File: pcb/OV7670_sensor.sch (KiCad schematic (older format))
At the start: 2 parts, among them U5 OV7670_module, U6 OV7670_module

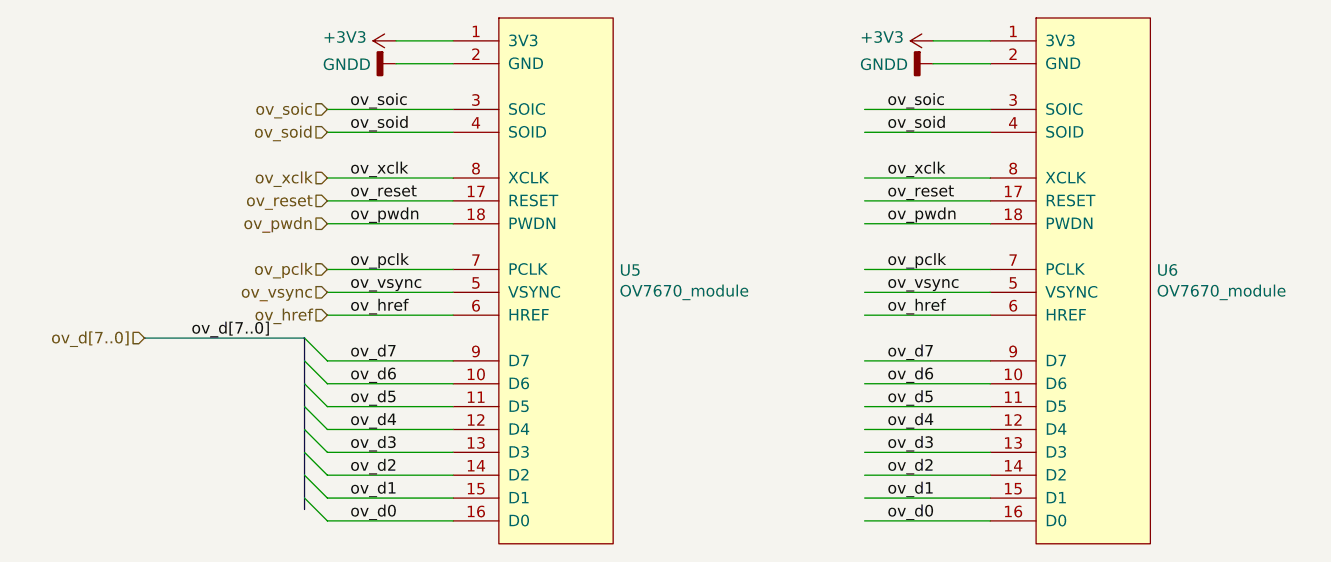
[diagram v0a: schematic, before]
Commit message: OV flat footprint
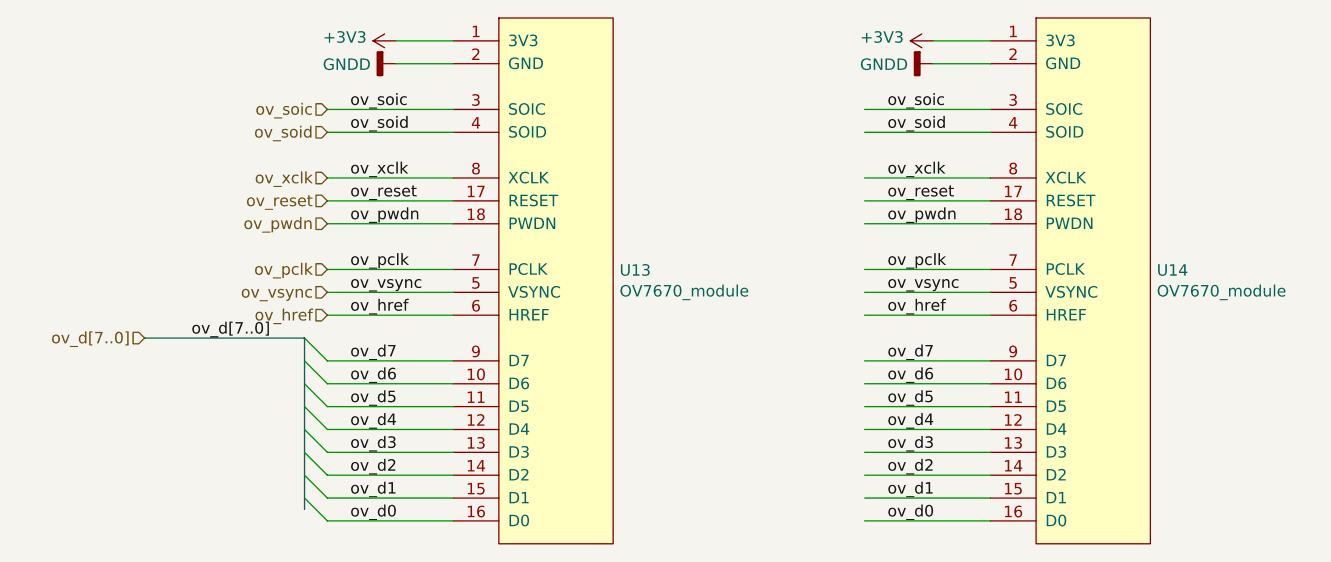
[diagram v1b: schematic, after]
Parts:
- U5: footprint Connector_PinSocket_2.54mm:PinSocket_2x09_P2.54mm_Horizontal -> OV7670_Module:OV7670_Flat
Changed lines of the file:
@@
 AR Path="/5C9B2A05/5C9B36DA" Ref="U5"  Part="1"
 AR Path="/5C9C0506/5C9B36DA" Ref="U7"  Part="1"
-AR Path="/5C9C8588/5C9B36DA" Ref="U?"  Part="1"
-AR Path="/5C9C95E9/5C9B36DA" Ref="U?"  Part="1"
-AR Path="/5C9CA91D/5C9B36DA" Ref="U?"  Part="1"
-AR Path="/5C9CA93A/5C9B36DA" Ref="U?"  Part="1"
-AR Path="/5C9CA957/5C9B36DA" Ref="U?"  Part="1"
-AR Path="/5C9CA974/5C9B36DA" Ref="U?"  Part="1"
-F 0 "U?" H 4578 3146 50  0000 L CNN
+AR Path="/5C9C8588/5C9B36DA" Ref="U9"  Part="1"
+AR Path="/5C9C95E9/5C9B36DA" Ref="U11"  Part="1"
+AR Path="/5C9CA91D/5C9B36DA" Ref="U13"  Part="1"
+AR Path="/5C9CA93A/5C9B36DA" Ref="U15"  Part="1"
+AR Path="/5C9CA957/5C9B36DA" Ref="U17"  Part="1"
+AR Path="/5C9CA974/5C9B36DA" Ref="U19"  Part="1"
+F 0 "U13" H 4578 3146 50  0000 L CNN
 F 1 "OV7670_module" H 4578 3055 50  0000 L CNN
-F 2 "Connector_PinSocket_2.54mm:PinSocket_2x09_P2.54mm_Horizontal" H 4150 4200 50  0001 C CNN
+F 2 "OV7670_Module:OV7670_Flat" H 4150 4200 50  0001 C CNN
 F 3 "" H 4150 4200 50  0001 C CNN
 	1    4150 2950
@@
 AR Path="/5C9B2A05/5C9B3748" Ref="#PWR0110"  Part="1"
 AR Path="/5C9C0506/5C9B3748" Ref="#PWR018"  Part="1"
-AR Path="/5C9C8588/5C9B3748" Ref="#PWR?"  Part="1"
-AR Path="/5C9C95E9/5C9B3748" Ref="#PWR?"  Part="1"
-AR Path="/5C9CA91D/5C9B3748" Ref="#PWR?"  Part="1"
-AR Path="/5C9CA93A/5C9B3748" Ref="#PWR?"  Part="1"
-AR Path="/5C9CA957/5C9B3748" Ref="#PWR?"  Part="1"
-AR Path="/5C9CA974/5C9B3748" Ref="#PWR?"  Part="1"
-F 0 "#PWR?" H 3600 1600 50  0001 C CNN
+AR Path="/5C9C8588/5C9B3748" Ref="#PWR0114"  Part="1"
+AR Path="/5C9C95E9/5C9B3748" Ref="#PWR0118"  Part="1"
+AR Path="/5C9CA91D/5C9B3748" Ref="#PWR0122"  Part="1"
+AR Path="/5C9CA93A/5C9B3748" Ref="#PWR0126"  Part="1"
+AR Path="/5C9CA957/5C9B3748" Ref="#PWR0130"  Part="1"
+AR Path="/5C9CA974/5C9B3748" Ref="#PWR0134"  Part="1"
+F 0 "#PWR0122" H 3600 1600 50  0001 C CNN
 F 1 "GNDD" V 3604 1740 50  0000 R CNN
 F 2 "" H 3600 1850 50  0001 C CNN
@@
 AR Path="/5C9B2A05/5C9B37B4" Ref="#PWR0111"  Part="1"
 AR Path="/5C9C0506/5C9B37B4" Ref="#PWR014"  Part="1"
-AR Path="/5C9C8588/5C9B37B4" Ref="#PWR?"  Part="1"
-AR Path="/5C9C95E9/5C9B37B4" Ref="#PWR?"  Part="1"
-AR Path="/5C9CA91D/5C9B37B4" Ref="#PWR?"  Part="1"
-AR Path="/5C9CA93A/5C9B37B4" Ref="#PWR?"  Part="1"
-AR Path="/5C9CA957/5C9B37B4" Ref="#PWR?"  Part="1"
-AR Path="/5C9CA974/5C9B37B4" Ref="#PWR?"  Part="1"
-F 0 "#PWR?" H 3600 1600 50  0001 C CNN
+AR Path="/5C9C8588/5C9B37B4" Ref="#PWR0115"  Part="1"
+AR Path="/5C9C95E9/5C9B37B4" Ref="#PWR0119"  Part="1"
+AR Path="/5C9CA91D/5C9B37B4" Ref="#PWR0123"  Part="1"
+AR Path="/5C9CA93A/5C9B37B4" Ref="#PWR0127"  Part="1"
+AR Path="/5C9CA957/5C9B37B4" Ref="#PWR0131"  Part="1"
+AR Path="/5C9CA974/5C9B37B4" Ref="#PWR0135"  Part="1"
+F 0 "#PWR0123" H 3600 1600 50  0001 C CNN
 F 1 "+3V3" V 3615 1878 50  0000 L CNN
 F 2 "" H 3600 1750 50  0001 C CNN
@@
 AR Path="/5C9B2A05/5C9B9810" Ref="U6"  Part="1"
 AR Path="/5C9C0506/5C9B9810" Ref="U8"  Part="1"
-AR Path="/5C9C8588/5C9B9810" Ref="U?"  Part="1"
-AR Path="/5C9C95E9/5C9B9810" Ref="U?"  Part="1"
-AR Path="/5C9CA91D/5C9B9810" Ref="U?"  Part="1"
-AR Path="/5C9CA93A/5C9B9810" Ref="U?"  Part="1"
-AR Path="/5C9CA957/5C9B9810" Ref="U?"  Part="1"
-AR Path="/5C9CA974/5C9B9810" Ref="U?"  Part="1"
-F 0 "U?" H 6928 3146 50  0000 L CNN
+AR Path="/5C9C8588/5C9B9810" Ref="U10"  Part="1"
+AR Path="/5C9C95E9/5C9B9810" Ref="U12"  Part="1"
+AR Path="/5C9CA91D/5C9B9810" Ref="U14"  Part="1"
+AR Path="/5C9CA93A/5C9B9810" Ref="U16"  Part="1"
+AR Path="/5C9CA957/5C9B9810" Ref="U18"  Part="1"
+AR Path="/5C9CA974/5C9B9810" Ref="U20"  Part="1"
+F 0 "U14" H 6928 3146 50  0000 L CNN
 F 1 "OV7670_module" H 6928 3055 50  0000 L CNN
 F 2 "Connector_PinSocket_2.54mm:PinSocket_2x09_P2.54mm_Vertical" H 6500 4200 50  0001 C CNN
@@
 AR Path="/5C9B2A05/5C9B9819" Ref="#PWR0112"  Part="1"
 AR Path="/5C9C0506/5C9B9819" Ref="#PWR020"  Part="1"
-AR Path="/5C9C8588/5C9B9819" Ref="#PWR?"  Part="1"
-AR Path="/5C9C95E9/5C9B9819" Ref="#PWR?"  Part="1"
-AR Path="/5C9CA91D/5C9B9819" Ref="#PWR?"  Part="1"
-AR Path="/5C9CA93A/5C9B9819" Ref="#PWR?"  Part="1"
-AR Path="/5C9CA957/5C9B9819" Ref="#PWR?"  Part="1"
-AR Path="/5C9CA974/5C9B9819" Ref="#PWR?"  Part="1"
-F 0 "#PWR?" H 5950 1600 50  0001 C CNN
+AR Path="/5C9C8588/5C9B9819" Ref="#PWR0116"  Part="1"
+AR Path="/5C9C95E9/5C9B9819" Ref="#PWR0120"  Part="1"
+AR Path="/5C9CA91D/5C9B9819" Ref="#PWR0124"  Part="1"
+AR Path="/5C9CA93A/5C9B9819" Ref="#PWR0128"  Part="1"
+AR Path="/5C9CA957/5C9B9819" Ref="#PWR0132"  Part="1"
+AR Path="/5C9CA974/5C9B9819" Ref="#PWR0136"  Part="1"
+F 0 "#PWR0124" H 5950 1600 50  0001 C CNN
 F 1 "GNDD" V 5954 1740 50  0000 R CNN
 F 2 "" H 5950 1850 50  0001 C CNN
@@
 AR Path="/5C9B2A05/5C9B981F" Ref="#PWR0113"  Part="1"
 AR Path="/5C9C0506/5C9B981F" Ref="#PWR019"  Part="1"
-AR Path="/5C9C8588/5C9B981F" Ref="#PWR?"  Part="1"
-AR Path="/5C9C95E9/5C9B981F" Ref="#PWR?"  Part="1"
-AR Path="/5C9CA91D/5C9B981F" Ref="#PWR?"  Part="1"
-AR Path="/5C9CA93A/5C9B981F" Ref="#PWR?"  Part="1"
-AR Path="/5C9CA957/5C9B981F" Ref="#PWR?"  Part="1"
-AR Path="/5C9CA974/5C9B981F" Ref="#PWR?"  Part="1"
-F 0 "#PWR?" H 5950 1600 50  0001 C CNN
+AR Path="/5C9C8588/5C9B981F" Ref="#PWR0117"  Part="1"
+AR Path="/5C9C95E9/5C9B981F" Ref="#PWR0121"  Part="1"
+AR Path="/5C9CA91D/5C9B981F" Ref="#PWR0125"  Part="1"
+AR Path="/5C9CA93A/5C9B981F" Ref="#PWR0129"  Part="1"
+AR Path="/5C9CA957/5C9B981F" Ref="#PWR0133"  Part="1"
+AR Path="/5C9CA974/5C9B981F" Ref="#PWR0137"  Part="1"
+F 0 "#PWR0125" H 5950 1600 50  0001 C CNN
 F 1 "+3V3" V 5965 1878 50  0000 L CNN
 F 2 "" H 5950 1750 50  0001 C CNN

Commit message: Cameras angled 22.5.
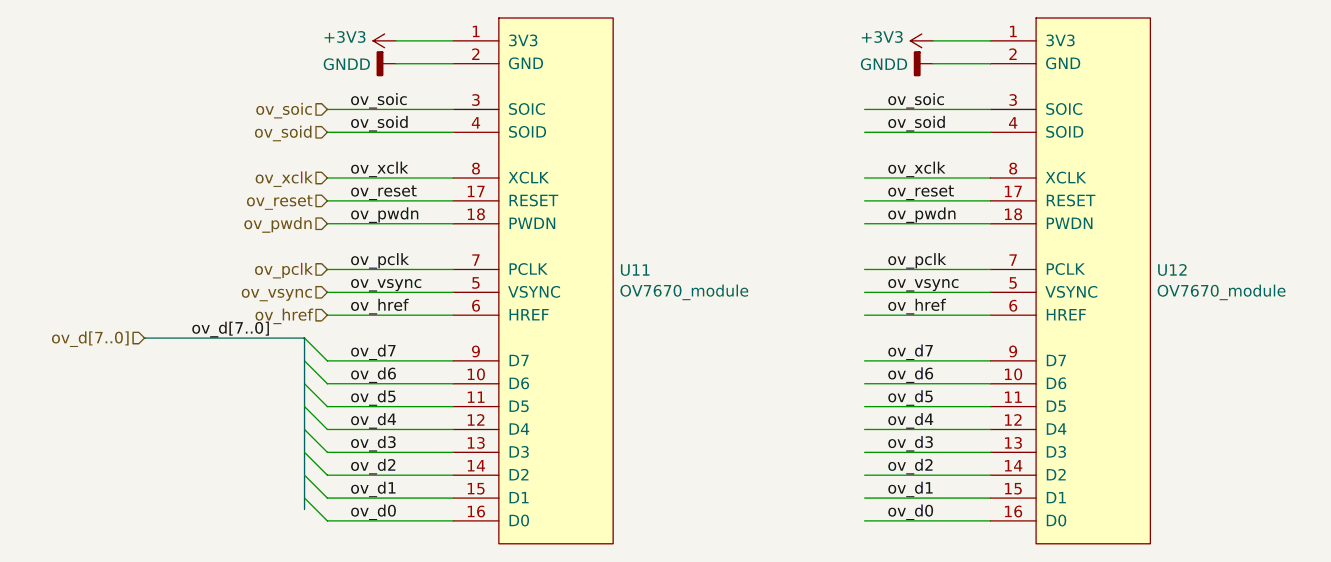
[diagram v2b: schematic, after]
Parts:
- U6: footprint Connector_PinSocket_2.54mm:PinSocket_2x09_P2.54mm_Vertical -> OV7670_Module:OV7670_Vertical
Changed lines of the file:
@@
 $Descr A4 11693 8268
 encoding utf-8
-Sheet 8 12
+Sheet 5 12
 Title ""
 Date ""
@@
 AR Path="/5C9CA957/5C9B36DA" Ref="U17"  Part="1"
 AR Path="/5C9CA974/5C9B36DA" Ref="U19"  Part="1"
-F 0 "U13" H 4578 3146 50  0000 L CNN
+F 0 "U11" H 4578 3146 50  0000 L CNN
 F 1 "OV7670_module" H 4578 3055 50  0000 L CNN
 F 2 "OV7670_Module:OV7670_Flat" H 4150 4200 50  0001 C CNN
@@
 AR Path="/5C9CA957/5C9B3748" Ref="#PWR0130"  Part="1"
 AR Path="/5C9CA974/5C9B3748" Ref="#PWR0134"  Part="1"
-F 0 "#PWR0122" H 3600 1600 50  0001 C CNN
+F 0 "#PWR0118" H 3600 1600 50  0001 C CNN
 F 1 "GNDD" V 3604 1740 50  0000 R CNN
 F 2 "" H 3600 1850 50  0001 C CNN
@@
 AR Path="/5C9CA957/5C9B37B4" Ref="#PWR0131"  Part="1"
 AR Path="/5C9CA974/5C9B37B4" Ref="#PWR0135"  Part="1"
-F 0 "#PWR0123" H 3600 1600 50  0001 C CNN
+F 0 "#PWR0119" H 3600 1600 50  0001 C CNN
 F 1 "+3V3" V 3615 1878 50  0000 L CNN
 F 2 "" H 3600 1750 50  0001 C CNN
@@
 AR Path="/5C9CA957/5C9B9810" Ref="U18"  Part="1"
 AR Path="/5C9CA974/5C9B9810" Ref="U20"  Part="1"
-F 0 "U14" H 6928 3146 50  0000 L CNN
+F 0 "U12" H 6928 3146 50  0000 L CNN
 F 1 "OV7670_module" H 6928 3055 50  0000 L CNN
-F 2 "Connector_PinSocket_2.54mm:PinSocket_2x09_P2.54mm_Vertical" H 6500 4200 50  0001 C CNN
+F 2 "OV7670_Module:OV7670_Vertical" H 6500 4200 50  0001 C CNN
 F 3 "" H 6500 4200 50  0001 C CNN
 	1    6500 2950
@@
 AR Path="/5C9CA957/5C9B9819" Ref="#PWR0132"  Part="1"
 AR Path="/5C9CA974/5C9B9819" Ref="#PWR0136"  Part="1"
-F 0 "#PWR0124" H 5950 1600 50  0001 C CNN
+F 0 "#PWR0120" H 5950 1600 50  0001 C CNN
 F 1 "GNDD" V 5954 1740 50  0000 R CNN
 F 2 "" H 5950 1850 50  0001 C CNN
@@
 AR Path="/5C9CA957/5C9B981F" Ref="#PWR0133"  Part="1"
 AR Path="/5C9CA974/5C9B981F" Ref="#PWR0137"  Part="1"
-F 0 "#PWR0125" H 5950 1600 50  0001 C CNN
+F 0 "#PWR0121" H 5950 1600 50  0001 C CNN
 F 1 "+3V3" V 5965 1878 50  0000 L CNN
 F 2 "" H 5950 1750 50  0001 C CNN

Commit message: Remove one flat sensor site.
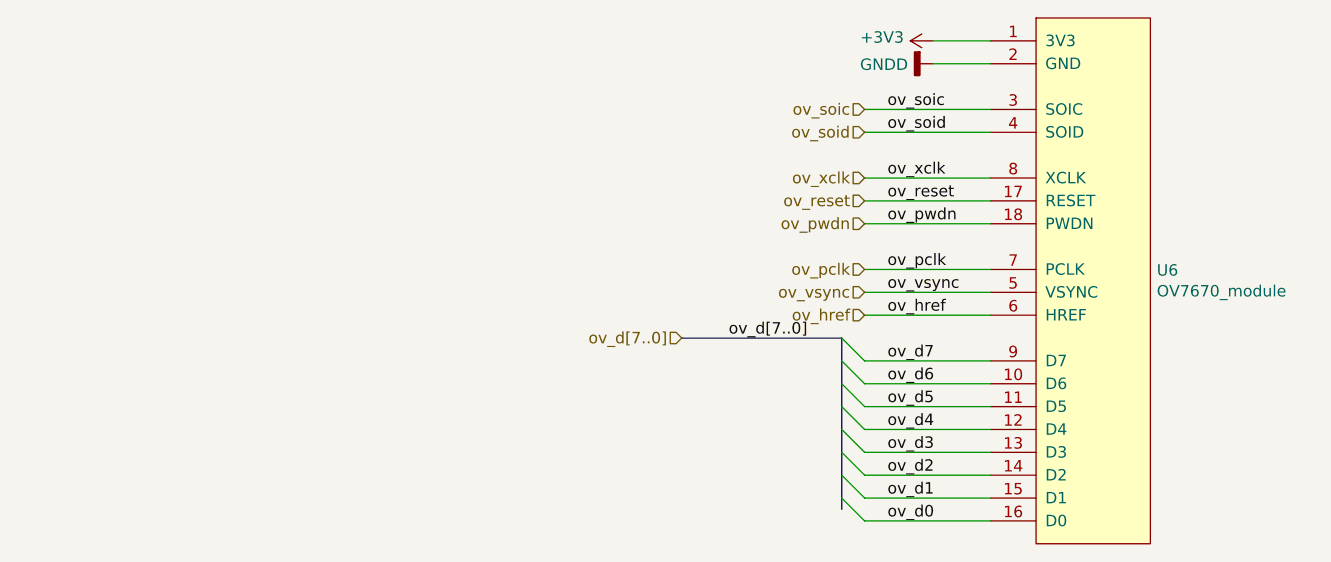
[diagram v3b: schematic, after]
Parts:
- removed U5: OV7670_module, OV7670_Module:OV7670_Flat, symbol OV7670:OV7670_module
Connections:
- wire segments 36 -> 18
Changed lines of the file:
@@
 $Descr A4 11693 8268
 encoding utf-8
-Sheet 5 12
+Sheet 5 11
 Title ""
 Date ""
@@
 Comment4 ""
 $EndDescr
-$Comp
-L OV7670:OV7670_module U5
-U 1 1 5C9B36DA
-P 4150 2950
-AR Path="/5C9B2A05/5C9B36DA" Ref="U5"  Part="1"
-AR Path="/5C9C0506/5C9B36DA" Ref="U7"  Part="1"
-AR Path="/5C9C8588/5C9B36DA" Ref="U9"  Part="1"
-AR Path="/5C9C95E9/5C9B36DA" Ref="U11"  Part="1"
-AR Path="/5C9CA91D/5C9B36DA" Ref="U13"  Part="1"
-AR Path="/5C9CA93A/5C9B36DA" Ref="U15"  Part="1"
-AR Path="/5C9CA957/5C9B36DA" Ref="U17"  Part="1"
-AR Path="/5C9CA974/5C9B36DA" Ref="U19"  Part="1"
-F 0 "U11" H 4578 3146 50  0000 L CNN
-F 1 "OV7670_module" H 4578 3055 50  0000 L CNN
-F 2 "OV7670_Module:OV7670_Flat" H 4150 4200 50  0001 C CNN
-F 3 "" H 4150 4200 50  0001 C CNN
-	1    4150 2950
-	1    0    0    -1
-$EndComp
-Wire Wire Line
-	3850 1750 3600 1750
-Wire Wire Line
-	3850 1850 3600 1850
-$Comp
-L power:GNDD #PWR0110
-U 1 1 5C9B3748
-P 3600 1850
-AR Path="/5C9B2A05/5C9B3748" Ref="#PWR0110"  Part="1"
-AR Path="/5C9C0506/5C9B3748" Ref="#PWR018"  Part="1"
-AR Path="/5C9C8588/5C9B3748" Ref="#PWR0114"  Part="1"
-AR Path="/5C9C95E9/5C9B3748" Ref="#PWR0118"  Part="1"
-AR Path="/5C9CA91D/5C9B3748" Ref="#PWR0122"  Part="1"
-AR Path="/5C9CA93A/5C9B3748" Ref="#PWR0126"  Part="1"
-AR Path="/5C9CA957/5C9B3748" Ref="#PWR0130"  Part="1"
-AR Path="/5C9CA974/5C9B3748" Ref="#PWR0134"  Part="1"
-F 0 "#PWR0118" H 3600 1600 50  0001 C CNN
-F 1 "GNDD" V 3604 1740 50  0000 R CNN
-F 2 "" H 3600 1850 50  0001 C CNN
-F 3 "" H 3600 1850 50  0001 C CNN
-	1    3600 1850
-	0    1    1    0
-$EndComp
-$Comp
-L power:+3V3 #PWR0111
-U 1 1 5C9B37B4
-P 3600 1750
-AR Path="/5C9B2A05/5C9B37B4" Ref="#PWR0111"  Part="1"
-AR Path="/5C9C0506/5C9B37B4" Ref="#PWR014"  Part="1"
-AR Path="/5C9C8588/5C9B37B4" Ref="#PWR0115"  Part="1"
-AR Path="/5C9C95E9/5C9B37B4" Ref="#PWR0119"  Part="1"
-AR Path="/5C9CA91D/5C9B37B4" Ref="#PWR0123"  Part="1"
-AR Path="/5C9CA93A/5C9B37B4" Ref="#PWR0127"  Part="1"
-AR Path="/5C9CA957/5C9B37B4" Ref="#PWR0131"  Part="1"
-AR Path="/5C9CA974/5C9B37B4" Ref="#PWR0135"  Part="1"
-F 0 "#PWR0119" H 3600 1600 50  0001 C CNN
-F 1 "+3V3" V 3615 1878 50  0000 L CNN
-F 2 "" H 3600 1750 50  0001 C CNN
-F 3 "" H 3600 1750 50  0001 C CNN
-	1    3600 1750
-	0    -1   -1   0
-$EndComp
-Wire Wire Line
-	3850 2050 3300 2050
-Wire Wire Line
-	3850 2150 3300 2150
-Text Label 3400 2050 0    50   ~ 0
-ov_soic
-Text Label 3400 2150 0    50   ~ 0
-ov_soid
-Wire Wire Line
-	3850 2350 3300 2350
-Text Label 3400 2350 0    50   ~ 0
-ov_xclk
-Wire Wire Line
-	3850 2450 3300 2450
-Text Label 3400 2450 0    50   ~ 0
-ov_reset
-Wire Wire Line
-	3850 2550 3300 2550
-Text Label 3400 2550 0    50   ~ 0
-ov_pwdn
-Wire Wire Line
-	3850 2750 3300 2750
-Wire Wire Line
-	3850 2850 3300 2850
-Wire Wire Line
-	3850 2950 3300 2950
-Wire Wire Line
-	3850 3150 3300 3150
-Text Label 3400 2750 0    50   ~ 0
+Text HLabel 5650 2750 0    50   Input ~ 0
 ov_pclk
-Text Label 3400 2850 0    50   ~ 0
-ov_vsync
-Text HLabel 3300 2750 0    50   Input ~ 0
-ov_pclk
-Text Label 3400 2950 0    50   ~ 0
-ov_href
-Text Label 3400 3150 0    50   ~ 0
-ov_d7
-Text Label 3050 3050 2    50   ~ 0
+Text Label 5400 3050 2    50   ~ 0
 ov_d[7..0]
 Entry Wire Line
-	3200 3050 3300 3150
-Wire Wire Line
-	3850 3250 3300 3250
-Text Label 3400 3250 0    50   ~ 0
-ov_d6
+	5550 3050 5650 3150
 Entry Wire Line
-	3200 3150 3300 3250
-Wire Wire Line
-	3850 3350 3300 3350
-Text Label 3400 3350 0    50   ~ 0
-ov_d5
+	5550 3150 5650 3250
 Entry Wire Line
-	3200 3250 3300 3350
-Wire Wire Line
-	3850 3450 3300 3450
-Text Label 3400 3450 0    50   ~ 0
-ov_d4
+	5550 3250 5650 3350
 Entry Wire Line
-	3200 3350 3300 3450
-Wire Wire Line
-	3850 3550 3300 3550
-Text Label 3400 3550 0    50   ~ 0
-ov_d3
+	5550 3350 5650 3450
 Entry Wire Line
-	3200 3450 3300 3550
-Wire Wire Line
-	3850 3650 3300 3650
-Text Label 3400 3650 0    50   ~ 0
-ov_d2
+	5550 3450 5650 3550
 Entry Wire Line
-	3200 3550 3300 3650
-Wire Wire Line
-	3850 3750 3300 3750
-Text Label 3400 3750 0    50   ~ 0
-ov_d1
+	5550 3550 5650 3650
 Entry Wire Line
-	3200 3650 3300 3750
-Wire Wire Line
-	3850 3850 3300 3850
-Text Label 3400 3850 0    50   ~ 0
-ov_d0
+	5550 3650 5650 3750
 Entry Wire Line
-	3200 3750 3300 3850
+	5550 3750 5650 3850
 Wire Bus Line
-	3200 3050 2500 3050
-Text HLabel 3300 2850 0    50   Input ~ 0
+	5550 3050 4850 3050
+Text HLabel 5650 2850 0    50   Input ~ 0
 ov_vsync
-Text HLabel 3300 2950 0    50   Input ~ 0
+Text HLabel 5650 2950 0    50   Input ~ 0
 ov_href
-Text HLabel 2500 3050 0    50   Input ~ 0
+Text HLabel 4850 3050 0    50   Input ~ 0
 ov_d[7..0]
-Text HLabel 3300 2050 0    50   Input ~ 0
+Text HLabel 5650 2050 0    50   Input ~ 0
 ov_soic
-Text HLabel 3300 2150 0    50   Input ~ 0
+Text HLabel 5650 2150 0    50   Input ~ 0
 ov_soid
-Text HLabel 3300 2350 0    50   Input ~ 0
+Text HLabel 5650 2350 0    50   Input ~ 0
 ov_xclk
-Text HLabel 3300 2450 0    50   Input ~ 0
+Text HLabel 5650 2450 0    50   Input ~ 0
 ov_reset
-Text HLabel 3300 2550 0    50   Input ~ 0
+Text HLabel 5650 2550 0    50   Input ~ 0
 ov_pwdn
 $Comp
@@
 AR Path="/5C9CA957/5C9B9810" Ref="U18"  Part="1"
 AR Path="/5C9CA974/5C9B9810" Ref="U20"  Part="1"
-F 0 "U12" H 6928 3146 50  0000 L CNN
+F 0 "U6" H 6928 3146 50  0000 L CNN
 F 1 "OV7670_module" H 6928 3055 50  0000 L CNN
 F 2 "OV7670_Module:OV7670_Vertical" H 6500 4200 50  0001 C CNN
@@
 AR Path="/5C9CA957/5C9B9819" Ref="#PWR0132"  Part="1"
 AR Path="/5C9CA974/5C9B9819" Ref="#PWR0136"  Part="1"
-F 0 "#PWR0120" H 5950 1600 50  0001 C CNN
+F 0 "#PWR0112" H 5950 1600 50  0001 C CNN
 F 1 "GNDD" V 5954 1740 50  0000 R CNN
 F 2 "" H 5950 1850 50  0001 C CNN
@@
 AR Path="/5C9CA957/5C9B981F" Ref="#PWR0133"  Part="1"
 AR Path="/5C9CA974/5C9B981F" Ref="#PWR0137"  Part="1"
-F 0 "#PWR0121" H 5950 1600 50  0001 C CNN
+F 0 "#PWR0113" H 5950 1600 50  0001 C CNN
 F 1 "+3V3" V 5965 1878 50  0000 L CNN
 F 2 "" H 5950 1750 50  0001 C CNN
@@
 ov_d0
 Wire Bus Line
-	3200 3050 3200 3800
+	5550 3050 5550 3800
 $EndSCHEMATC
